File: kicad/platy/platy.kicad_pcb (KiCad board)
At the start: 2 copper layers, 100 x 100 mm, 89 parts, among them J1 Conn_01x04_Socket, J2 Conn_01x02_Socket, J5 USB_C_Receptacle_USB2.0_16P, J6 Conn_01x04_Pin, J8 Conn_01x14_Socket, J9 Conn_02x04_Odd_Even, Q4 BC847, Q5 Q_PMOS_GSD, SW2 SW_Push(Boot), SW3 SW_Push(EN), U10 ESP32-S3-WROOM-1, U4 CC1101, U5 PN5321A3HN_C1xx, U6 TSOP382xx, U7 AMS1117-3.3, Y2 27.12Mhz, Y3 26MHz

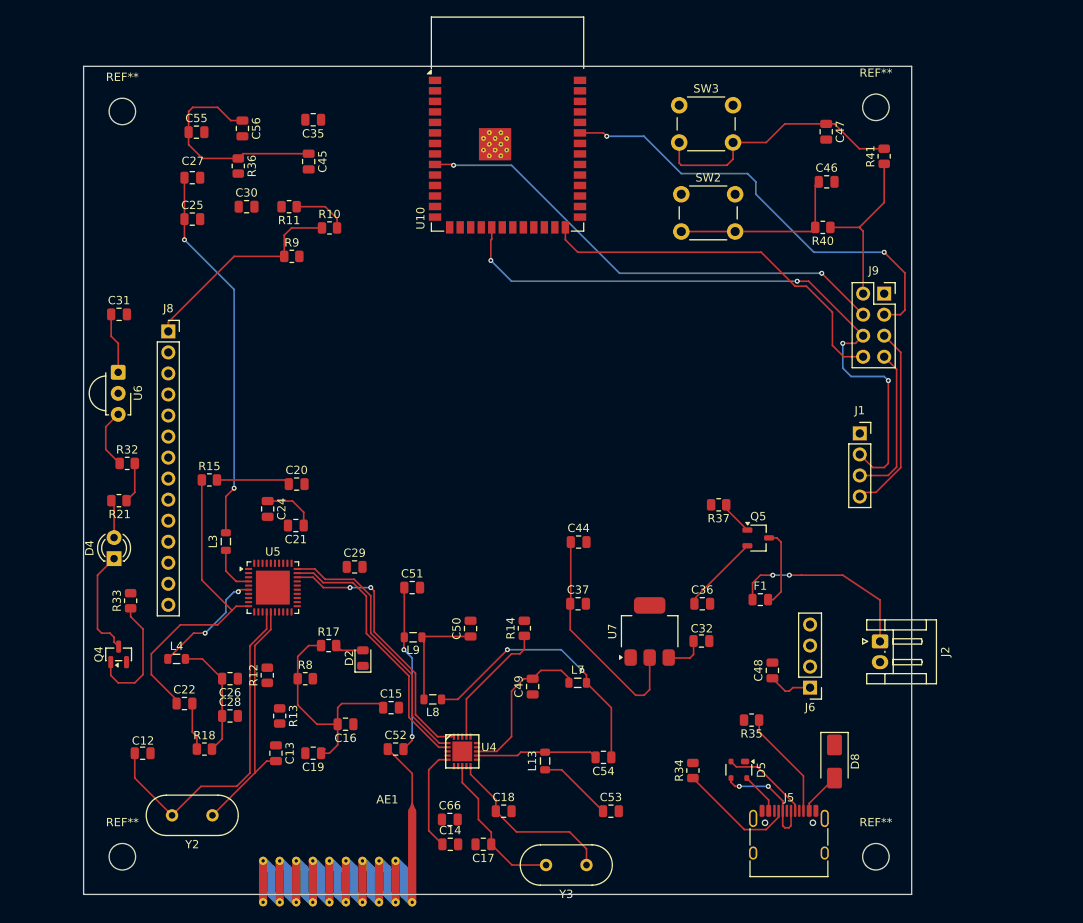
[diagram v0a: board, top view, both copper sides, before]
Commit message: Completed the most of the routing
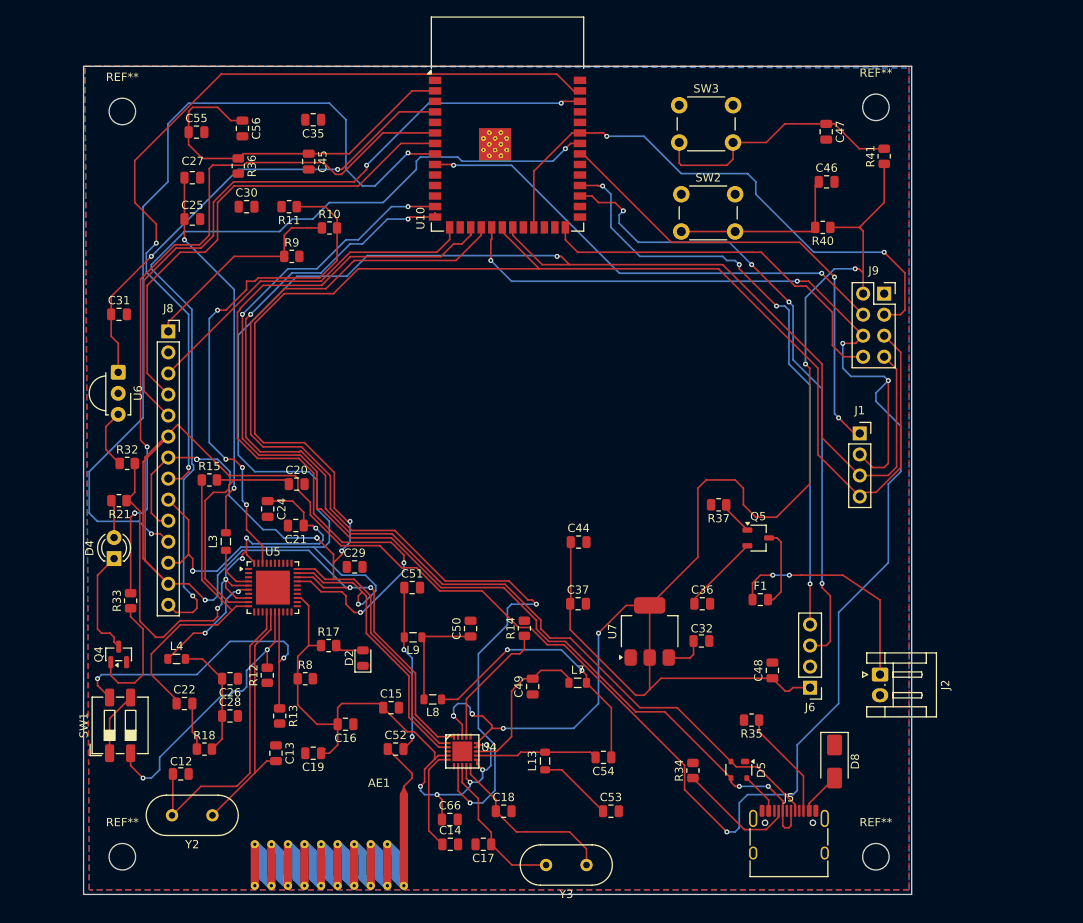
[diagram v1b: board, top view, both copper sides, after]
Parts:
- added SW1: SW_DPST, Button_Switch_SMD:SW_DIP_SPSTx02_Slide_6.7x6.64mm_W6.73mm_P2.54mm_LowProfile_JPin, F.Cu at (107.2, 129.1)
- moved C12 5.24 mm to (114.5, 135.0)
- moved J2 4.00 mm to (199.0, 123.0)
- moved AE1 2.24 mm to (132.5, 142.7)
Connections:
- J8 pad 8: /MISO -> /led
- J8 pad 9: /3v3 -> /MISO
- R8 pad 2: unconnected-(R8-Pad2) -> /SSEL/SCL/RX
- R9 pad 2: unconnected-(R9-Pad2) -> /SSEL/SCL/RX
- U10 pad 39: unconnected-(U10-IO1-Pad39) -> /led
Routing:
- net /3v3: track 146.3 -> 411.0 mm, vias 0 -> 19
- net /MOSI: track 111.8 -> 341.7 mm, vias 6 -> 8
- net /MISO: track 51.2 -> 234.3 mm, vias 0 -> 4
- net /SCK: track 55.6 -> 232.6 mm, vias 0 -> 7
- net /CSn: track 0.00 -> 128.7 mm, vias 0 -> 2
- net /USB_D-: track 13.7 -> 136.6 mm, vias 2 -> 4
- net /USB_D+: track 10.7 -> 131.3 mm, vias 0 -> 2
- net /irq_tht: track 0.00 -> 107.6 mm, vias 0 -> 2
- net /CSN: track 0.00 -> 104.6 mm, vias 0 -> 2
- net /led: track 0.00 -> 103.0 mm, vias 0 -> 2
- net /SSEL: track 0.00 -> 97.1 mm, vias 0 -> 2
- net /gpio 6: track 0.00 -> 88.4 mm, vias 0 -> 3
- net /d/c: track 0.00 -> 81.8 mm, vias 0 -> 2
- net /Vrx: track 0.00 -> 77.8 mm, vias 0 -> 4
- net /Vry: track 0.00 -> 73.2 mm, vias 0 -> 4
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- added copper zone on B.Cu, net GND
- added copper zone on F.Cu, net GND

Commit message: made the second ertation of the pcb
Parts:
- removed REF** (x4): MountingHole_3.2mm_M3, MountingHole:MountingHole_3.2mm_M3
- J5: footprint Connector_USB:USB_C_Receptacle_HRO_TYPE-C-31-M-12 -> Connector_USB:USB_C_Receptacle_GCT_USB4105-xx-A_16P_TopMnt_Horizontal
- moved Q4 113.8 mm to (216.6, 89.5), turned to 0 degrees
- moved D4 113.4 mm to (217.5, 85.8)
- moved U6 111.8 mm to (218.0, 99.6), turned to 90 degrees
- moved R21 108.8 mm to (213.5, 79.5), turned to 0 degrees
- moved R33 105.4 mm to (209.5, 84.0), turned to 180 degrees
- moved C31 104.9 mm to (208.5, 106.5), turned to 90 degrees
- moved R32 102.5 mm to (210.5, 101.5), turned to 180 degrees
- moved D8 98.5 mm to (119.0, 69.0)
- moved J9 95.8 mm to (108.6, 107.0), turned to 60 degrees
- moved J5 94.8 mm to (131.1, 67.7), turned to 180 degrees
- moved D5 85.9 mm to (123.0, 72.0), turned to 90 degrees
- moved R35 84.4 mm to (118.6, 74.5)
- moved Y3 83.0 mm to (110.4, 82.2), turned to 120 degrees
- moved R34 77.8 mm to (121.9, 79.0), turned to 180 degrees
- moved SW1 76.2 mm to (177.1, 98.8), turned to 180 degrees
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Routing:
- net /MOSI: track 341.7 -> 178.6 mm, vias 8 -> 10
- net /3v3: track 411.0 -> 287.8 mm, vias 19 -> 24
- net /USB_D+: track 131.3 -> 46.4 mm
- net /SSEL: track 97.1 -> 24.5 mm, vias 2 -> 3
- net /USB_D-: track 136.6 -> 64.1 mm
- net /SCK: track 232.6 -> 169.3 mm, vias 7 -> 5
- net /CSN: track 104.6 -> 42.0 mm
- net /CSn: track 128.7 -> 67.3 mm, vias 2 -> 7
- net /MISO: track 234.3 -> 173.3 mm, vias 4 -> 9
- net /led: track 103.0 -> 57.9 mm, vias 2 -> 4
- net /irq_tht: track 107.6 -> 65.2 mm
- net /GPIO 4: track 57.9 -> 94.8 mm, vias 2 -> 8
- net /IRQ: track 45.7 -> 82.6 mm, vias 0 -> 2
- net /Vrx: track 77.8 -> 42.6 mm, vias 4 -> 2
- net /CE: track 68.6 -> 101.9 mm, vias 2 -> 3
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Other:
- board size 100 x 100 mm -> 125.8 x 52.6 mm

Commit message: updated pcb
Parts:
- added J3: Conn_Coaxial, Connector_Coaxial:U.FL_Molex_MCRF_73412-0110_Vertical, F.Cu at (187.7, 110.4)
- AE1: footprint RF_Antenna:Texas_SWRA416_868MHz_915MHz -> Connector_Coaxial:SMA_Amphenol_132134_Vertical
- Y2, Y3: footprint Crystal:Crystal_HC49-U_Vertical -> Crystal:Crystal_SMD_5032-2Pin_5.0x3.2mm
- moved C30 33.0 mm to (170.6, 112.5), turned to 90 degrees
- moved C29 30.6 mm to (167.8, 112.4), turned to 90 degrees
- moved L7 24.5 mm to (102.1, 102.6)
- moved C49 22.5 mm to (114.7, 100.2), turned to 90 degrees
- moved L8 21.4 mm to (101.0, 99.2), turned to 180 degrees
- moved Y2 21.2 mm to (153.5, 109.3), turned to -90 degrees
- moved C18 19.4 mm to (107.7, 93.5), turned to 180 degrees
- moved L9 18.5 mm to (100.8, 93.9), turned to 90 degrees
- moved C50 17.9 mm to (104.8, 96.1)
- moved C51 17.6 mm to (104.9, 91.3)
- moved C54 17.5 mm to (109.0, 96.7)
- moved C52 16.8 mm to (102.2, 87.9), turned to -90 degrees
- moved J6 15.1 mm to (197.7, 114.4), turned to 120 degrees
- moved AE1 14.8 mm to (105.6, 79.7)
- moved L13 13.9 mm to (110.0, 100.1)
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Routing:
- net GND: track 18.2 -> 363.5 mm, vias 2 -> 1165
- net /3v3: track 287.8 -> 378.3 mm, vias 24 -> 32
- net Net-(U4-XOSC_Q1): track 32.1 -> 7.13 mm, vias 2 -> 0
- net Net-(U4-XOSC_Q2): track 29.3 -> 6.51 mm, vias 2 -> 0
- net /Vrx: track 42.6 -> 62.1 mm
- net /Vry: track 42.3 -> 58.1 mm, vias 0 -> 1
- net Net-(U5-OSCOUT): track 33.6 -> 47.3 mm, vias 2 -> 3
- net /MOSI: track 178.6 -> 166.7 mm, vias 10 -> 9
- net Net-(C50-Pad1): track 19.6 -> 8.19 mm, vias 2 -> 0
- net /SCK: track 169.3 -> 160.1 mm, vias 5 -> 9
- net /MISO: track 173.3 -> 164.7 mm, vias 9 -> 8
- net Net-(U4-RF_P): track 18.8 -> 10.2 mm
- net Net-(D8-A): track 20.1 -> 26.1 mm, vias 0 -> 2
- net Net-(AE1-A): track 3.82 -> 8.62 mm
- net Net-(U5-OSCIN): track 7.74 -> 11.7 mm
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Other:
- board text added: "HARSH THORAT (harshthorat-cpu)"
- board text added: "LUCKY BELEL"

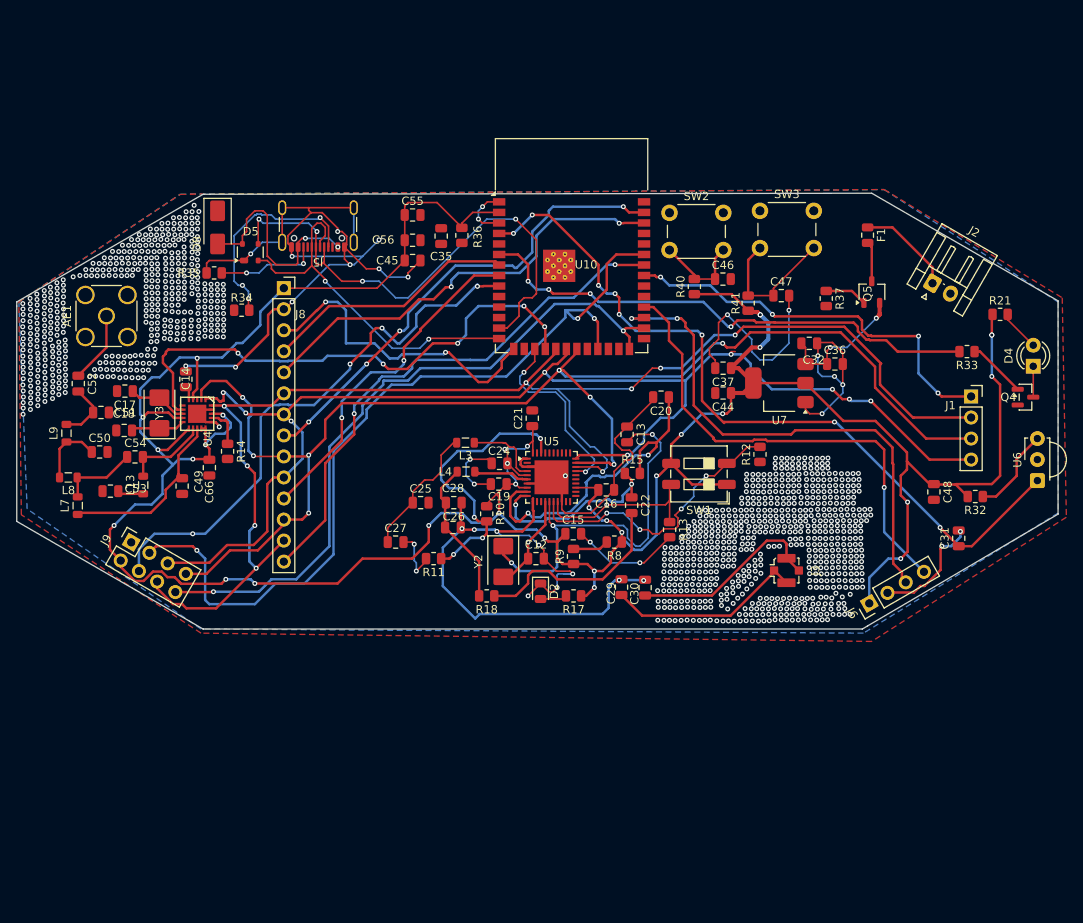
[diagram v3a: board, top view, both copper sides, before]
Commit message: changes made in the routing of the pcb
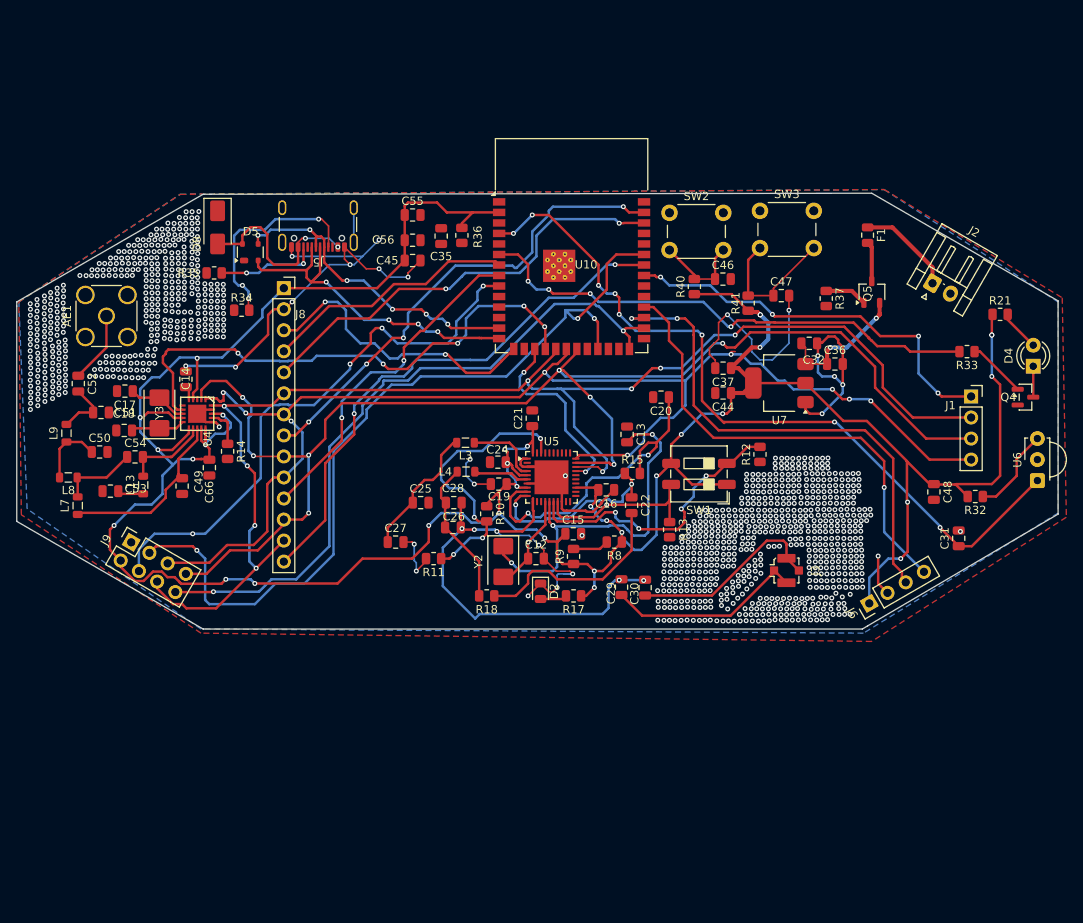
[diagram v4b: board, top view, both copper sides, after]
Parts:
- moved C24 0.25 mm to (152.8, 97.3)
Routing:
- net GND: track 363.5 -> 281.0 mm, vias 1165 -> 1121
- net /USB_D-: track 63.4 -> 38.4 mm, vias 4 -> 6
- net Net-(D8-A): track 26.1 -> 22.8 mm
- net /3v3: track 378.3 -> 381.1 mm
- net /cs_tht: track 38.3 -> 35.6 mm
- net /USB_D+: track 44.2 -> 41.7 mm, vias 2 -> 4
- net Net-(U5-OSCOUT): track 47.3 -> 45.4 mm
- net /Vry: track 58.1 -> 57.0 mm
- net /Vrx: track 62.1 -> 61.3 mm
- net Net-(J5-CC1): track 26.0 -> 25.3 mm
- net /SD_cs: track 48.7 -> 48.0 mm
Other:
- board text added: "HARSH THORAT"
- board text removed: "HARSH THORAT (harshthorat-cpu)"

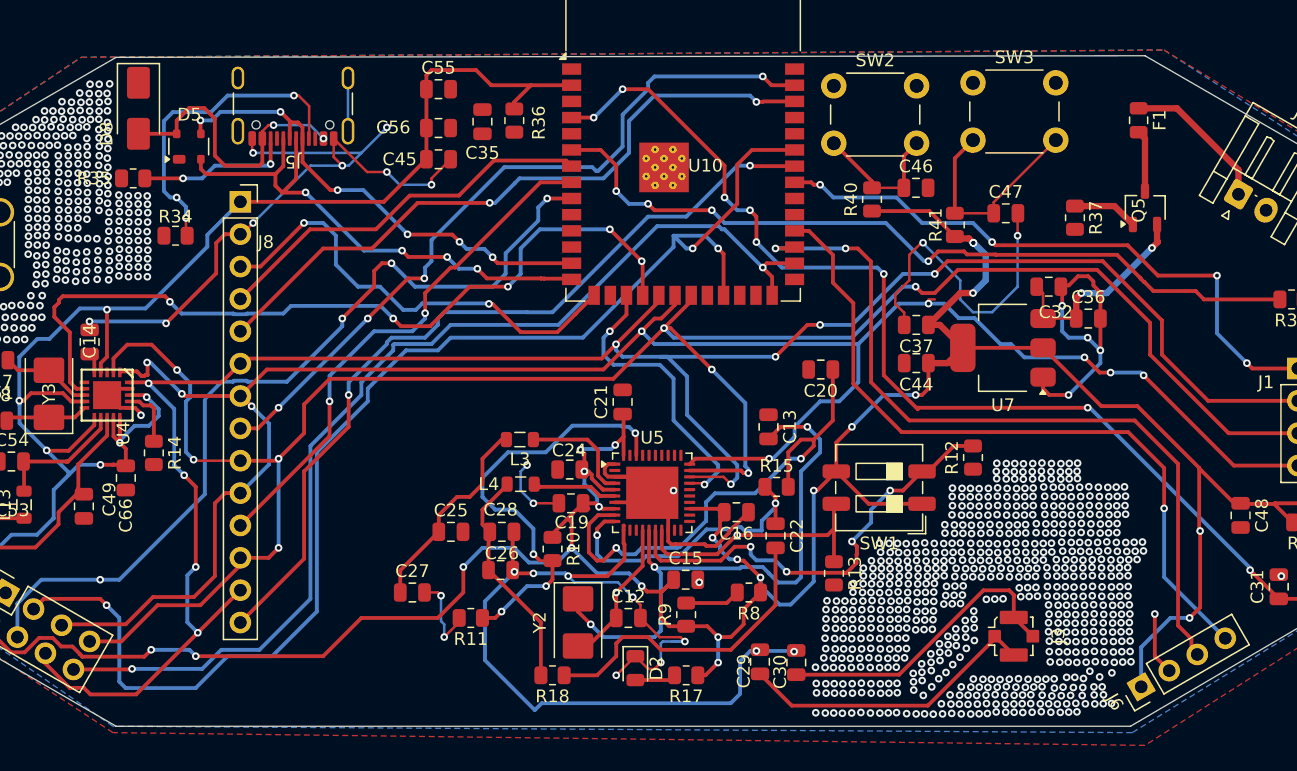
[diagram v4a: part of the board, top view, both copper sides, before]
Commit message: changes the made in the routing and in the schiematic and also in the value in the component
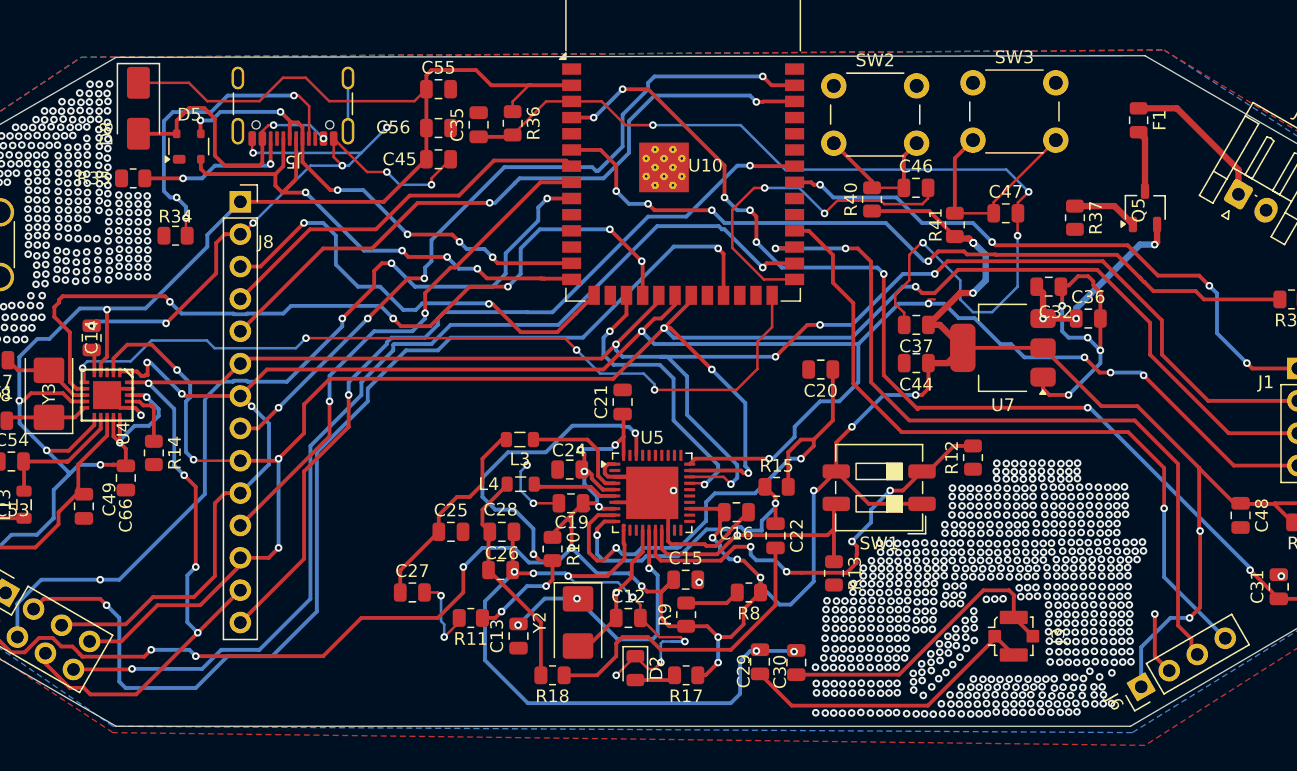
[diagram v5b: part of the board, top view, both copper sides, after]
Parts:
- C12, C13: value 22uF -> 22pF
- moved C13 25.6 mm to (148.8, 110.4), turned to 90 degrees
- moved C35 0.38 mm to (145.7, 70.3)
- moved C14 0.36 mm to (115.3, 87.0)
- moved R36 0.25 mm to (148.4, 70.2)
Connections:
- D8 pad 1: /5V -> /3v3
- U10 pad 26: /IRQ -> /GDO0
- U10 pad 35: /CE -> unconnected-(U10-IO42-Pad35)
- U4 pad 6: unconnected-(U4-GDO0-Pad6) -> /GDO0
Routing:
- net GND: track 281.0 -> 357.1 mm, vias 1121 -> 1125
- net /GDO0: track 0.00 -> 64.6 mm, vias 0 -> 4
- net /3v3: track 381.1 -> 406.4 mm
- net Net-(U5-OSCOUT): track 45.4 -> 21.8 mm
- net /CE: track 102.2 -> 86.1 mm, vias 3 -> 2
- net /IRQ: track 82.8 -> 80.3 mm
- net /SD_cs: track 48.0 -> 47.2 mm
- net /Vin: track 16.5 -> 16.7 mm, vias 2 -> 3

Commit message: corrected the boot and the enable and other things also
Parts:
- moved C14 0.71 mm to (114.8, 86.5)
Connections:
- C35 pad 1: GND -> /EN
- C46 pad 1: Net-(C46-Pad1) -> /BOOT
- C47 pad 1: Net-(C47-Pad1) -> /EN
- R36 pad 2: GND -> /EN
- R40 pad 2: Net-(C46-Pad1) -> /BOOT
- R41 pad 2: Net-(C47-Pad1) -> /EN
- SW2 pad 2: Net-(C46-Pad1) -> /BOOT
- SW3 pad 2: Net-(C47-Pad1) -> /EN
- U10 pad 16: unconnected-(U10-IO46-Pad16) -> /gdo2
- U10 pad 27: GND -> /BOOT
- U10 pad 3: GND -> /EN
- U4 pad 3: unconnected-(U4-GDO2-Pad3) -> /gdo2
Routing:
- net GND: track 357.1 -> 282.3 mm, vias 1125 -> 1122
- net /EN: track 0.00 -> 66.2 mm, vias 0 -> 1
- net /gdo2: track 0.00 -> 50.6 mm, vias 0 -> 2
- net /BOOT: track 0.00 -> 34.9 mm, vias 0 -> 3
- net Net-(C47-Pad1): track 17.1 -> 0.00 mm
- net Net-(C46-Pad1): track 11.2 -> 0.00 mm
- net Net-(U4-DCOUPL): track 1.81 -> 2.57 mm
